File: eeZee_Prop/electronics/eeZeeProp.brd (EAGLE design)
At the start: 47.2 x 24.4 mm, 33 parts, among them Q1 5MHz, Q2 2N3904SMD, SW1 RESET, U1 P8X32A-Q44, U2 24LC256-I/ST, U3 NCP1117 3V3

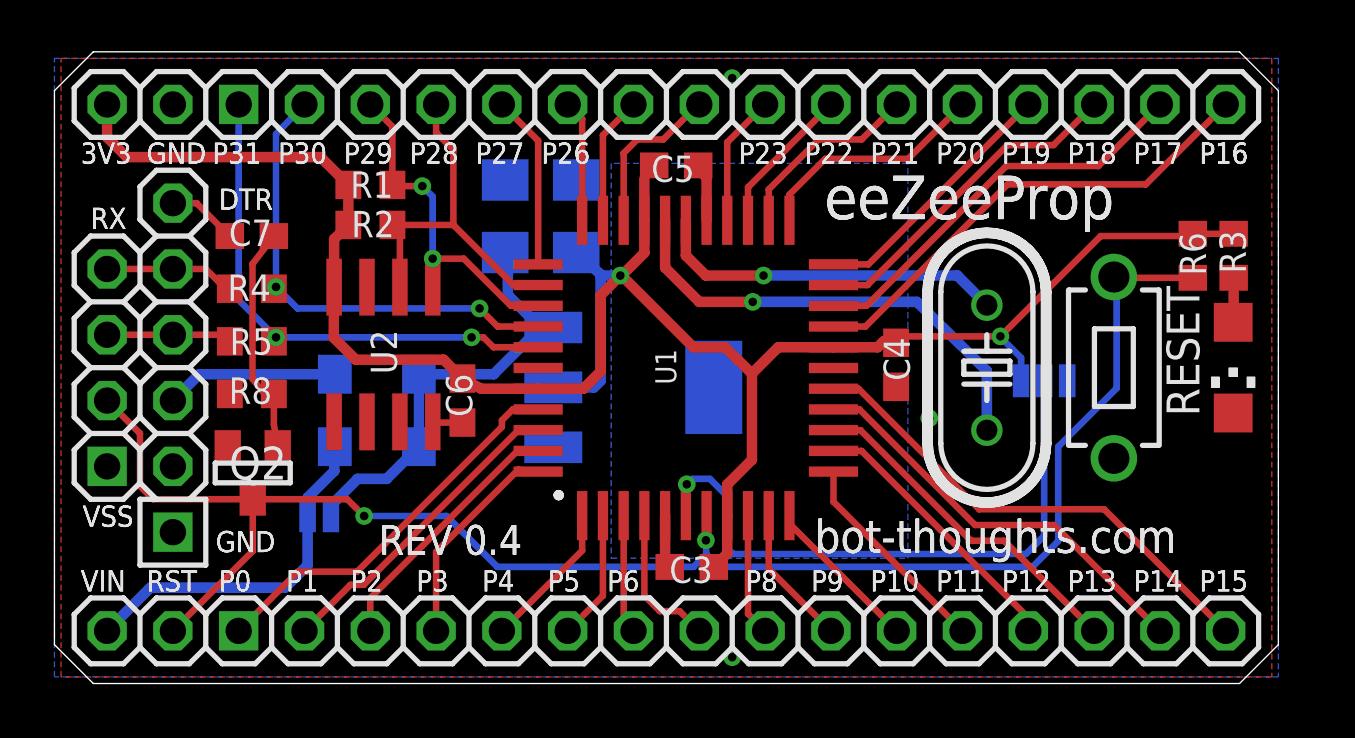
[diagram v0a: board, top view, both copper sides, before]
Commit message: Added regulator bypass option for 3.3V FTDI. Increased diode pad sizes.
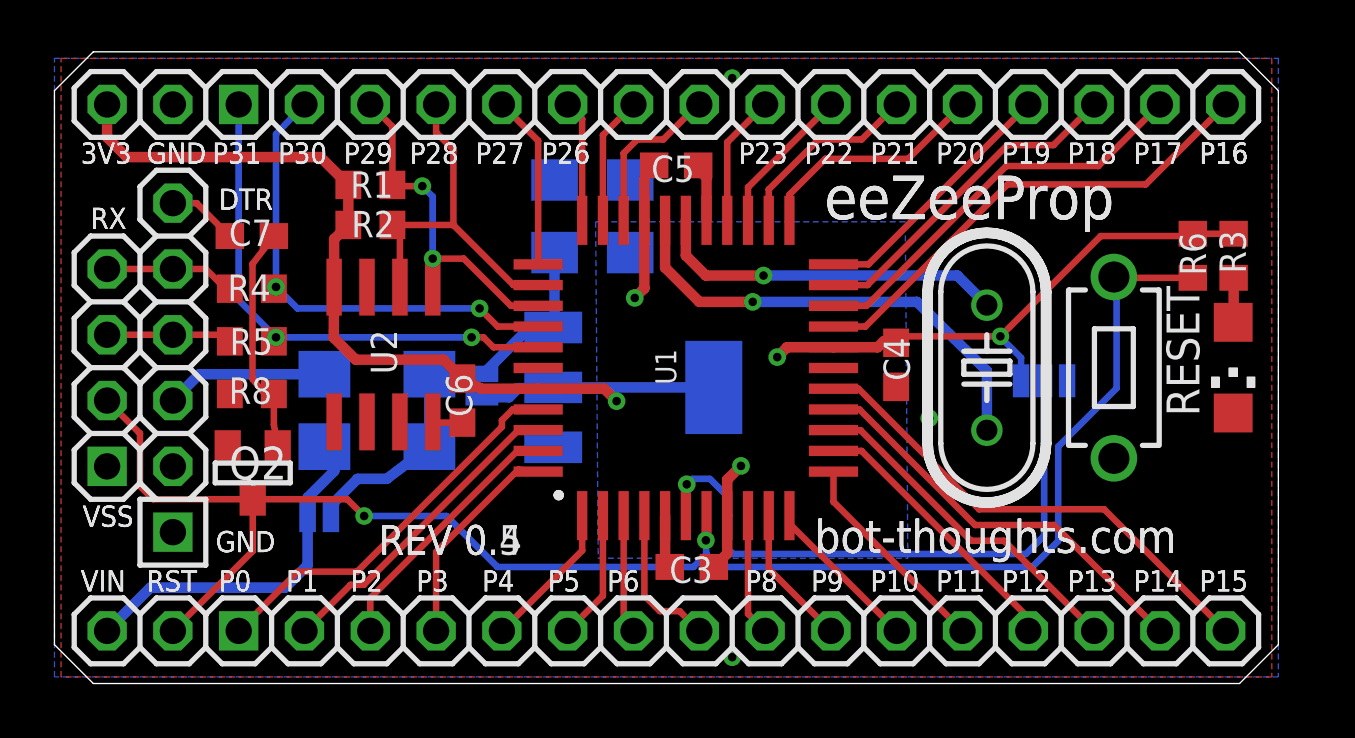
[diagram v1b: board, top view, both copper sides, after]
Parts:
- added SJ3: 3V3FTDI, SparkFun:SJ_2S-NO
- D1, D2: device mes_diode:SOD123FL -> bt_diode:SOD123FL
- moved C2 2.08 mm to (22.2, 18.0)
- moved C1 1.90 mm to (19.3, 18.0)
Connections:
- removed net HEATSINK: U3.4
- net V+: now also SJ3.2
- net VDD: now also SJ3.1, U3.4
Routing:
- net VDD: track 83.5 -> 70.5 mm, vias 2 -> 5
- net V+: track 16.9 -> 16.3 mm
- added copper zone on layer 16, net VDD
- removed copper zone on layer 16, net HEATSINK
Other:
- board text added: "REV 0.5"

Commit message: Fixed silkscreen conflicts. Enlarged DTR/GND labels. Moved other silk labels to different layer, disabled bottom name silk gen.
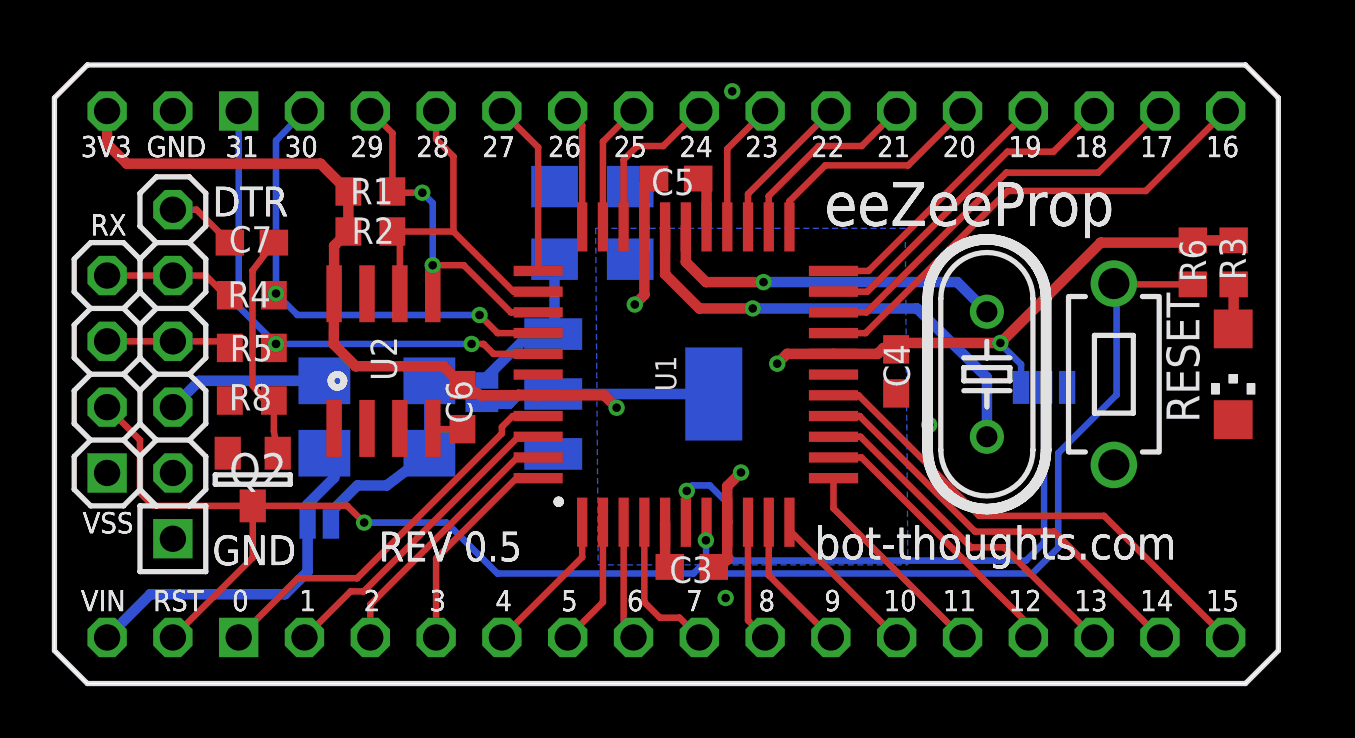
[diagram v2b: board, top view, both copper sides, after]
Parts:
- Q2: device mes_transistors:SOT-23 -> bt_transistor:SOT-23
- moved C5 0.51 mm to (24.0, 19.5)
- moved C6 0.25 mm to (15.7, 10.7)
- moved D1 0.25 mm to (12.4, 11.7)
- moved JP1 0.25 mm to (26.2, 22.1), flipped to the bottom, turned to 180 degrees
- moved JP6 0.25 mm to (4.57, 22.1), flipped to the bottom
- moved JP8 0.25 mm to (2.03, 22.1), flipped to the bottom
- moved R1 0.25 mm to (12.2, 19.0)
- moved R3 0.25 mm to (45.5, 16.3)
- moved R6 0.25 mm to (43.9, 16.3)
- moved Q2 0.25 mm to (7.63, 7.87)
- moved SJ1 0.25 mm to (10.2, 6.22)
- moved JP2 0.25 mm to (2.03, 1.78), flipped to the bottom
- moved JP5 0.25 mm to (26.2, 1.78), flipped to the bottom, turned to 180 degrees
- moved JP7 0.25 mm to (4.57, 1.78), flipped to the bottom
- moved C4 0.25 mm to (32.5, 12.0)
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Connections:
- net N$34 renamed RXI
- net N$35 renamed TXO
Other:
- board size 47.2 x 24.4 mm -> 47.2 x 23.9 mm
- board text added: "0"
- board text added: "1"
- board text added: "10"
- board text added: "11"
- board text added: "12"
- board text added: "13"
- board text added: "14"
- board text added: "15"
- board text added: "16"
- board text added: "17"
- board text added: "18"
- board text added: "19"
- board text added: "2"
- board text added: "20"
- board text added: "21"
- board text added: "22"
- board text added: "23"
- board text added: "24"
- board text added: "25"
- board text added: "26"
- board text added: "27"
- board text added: "28"
- board text added: "29"
- board text added: "3"
- board text added: "30"
- board text added: "31"
- board text added: "3V3FTDI"
- board text added: "4"
- board text added: "5"
- board text added: "6"
- board text added: "7"
- board text added: "8"
- board text added: "9"
- board text added: "License: CC-BY-SA"
- board text removed: "P0"
- board text removed: "P1"
- board text removed: "P10"
- board text removed: "P11"
- board text removed: "P12"
- board text removed: "P13"
- board text removed: "P14"
- board text removed: "P15"
- board text removed: "P16"
- board text removed: "P17"
- board text removed: "P18"
- board text removed: "P19"
- board text removed: "P2"
- board text removed: "P20"
- board text removed: "P21"
- board text removed: "P22"
- board text removed: "P23"
- board text removed: "P26"
- board text removed: "P27"
- board text removed: "P28"
- board text removed: "P29"
- board text removed: "P3"
- board text removed: "P30"
- board text removed: "P31"
- board text removed: "P4"
- board text removed: "P5"
- board text removed: "P6"
- board text removed: "P8"
- board text removed: "P9"
- board text removed: "REV 0.4"
- board text removed: "U3"

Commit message: Revised diode placement, silk, pin 1 dot on propeller.
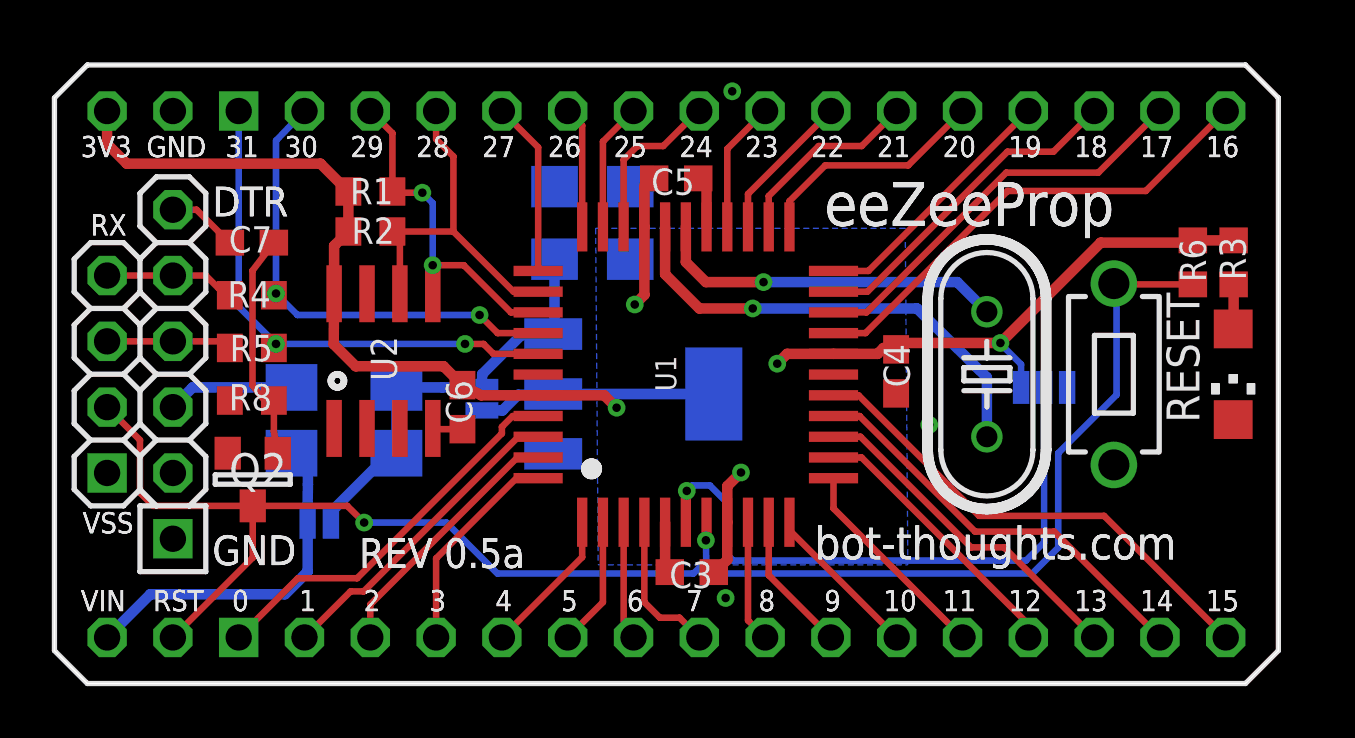
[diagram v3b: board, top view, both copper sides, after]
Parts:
- Q2: value 2N3904SMD -> 2N3904SOT23
- moved D1 1.30 mm to (11.2, 11.4)
- moved D2 1.27 mm to (11.2, 8.89)
- moved SJ3 0.25 mm to (16.5, 11.0)
- moved C3 0.20 mm to (24.6, 4.30)
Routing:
- net VUSB: track 6.27 -> 4.89 mm
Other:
- board text added: "REV 0.5a"
- board text removed: "REV 0.5"

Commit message: Changed to 8mil spacing, revised all PTH pins to octagon, relocated traces, vias for clearance. Resized traces with clearance problems.
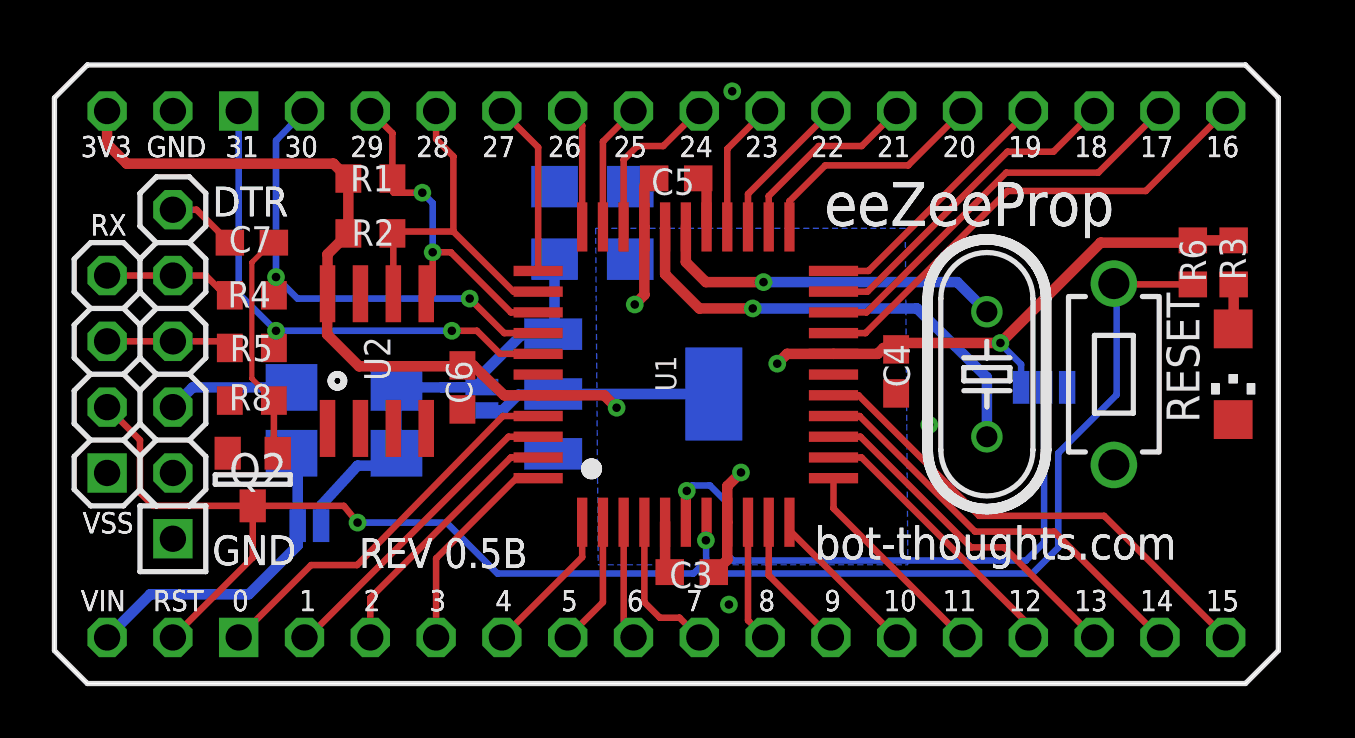
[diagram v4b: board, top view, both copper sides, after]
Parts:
- moved C6 0.76 mm to (15.7, 11.4)
- moved R1 0.50 mm to (12.2, 19.5)
- moved SJ1 0.40 mm to (9.84, 6.10)
- moved U2 0.25 mm to (12.4, 12.4)
- moved R2 0.07 mm to (12.2, 17.4)
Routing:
- net VIN: track 14.0 -> 12.5 mm
- net GND: track 5.69 -> 4.40 mm
- net V+: track 16.7 -> 17.4 mm
- net N$31: track 9.60 -> 8.91 mm
- net VDD: track 70.7 -> 71.2 mm
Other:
- board text added: "REV 0.5B"
- board text removed: "REV 0.5a"
